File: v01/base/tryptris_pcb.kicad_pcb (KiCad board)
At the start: 2 copper layers, 298.8 x 122 mm, 141 parts, among them J1 USB_C_Receptacle_USB2.0, J2 I2C-L, J3 I2C-R, SW1 Reset, U1 ATmega32U4-AU, U2 MCP23017_SO, U4 HOLE, Y1 16Mhz

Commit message: Clean up base silk screen too.
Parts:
- moved G*** 1.35 mm to (251.4, 88.2)
- moved G*** 0.64 mm to (100.6, 88.5)

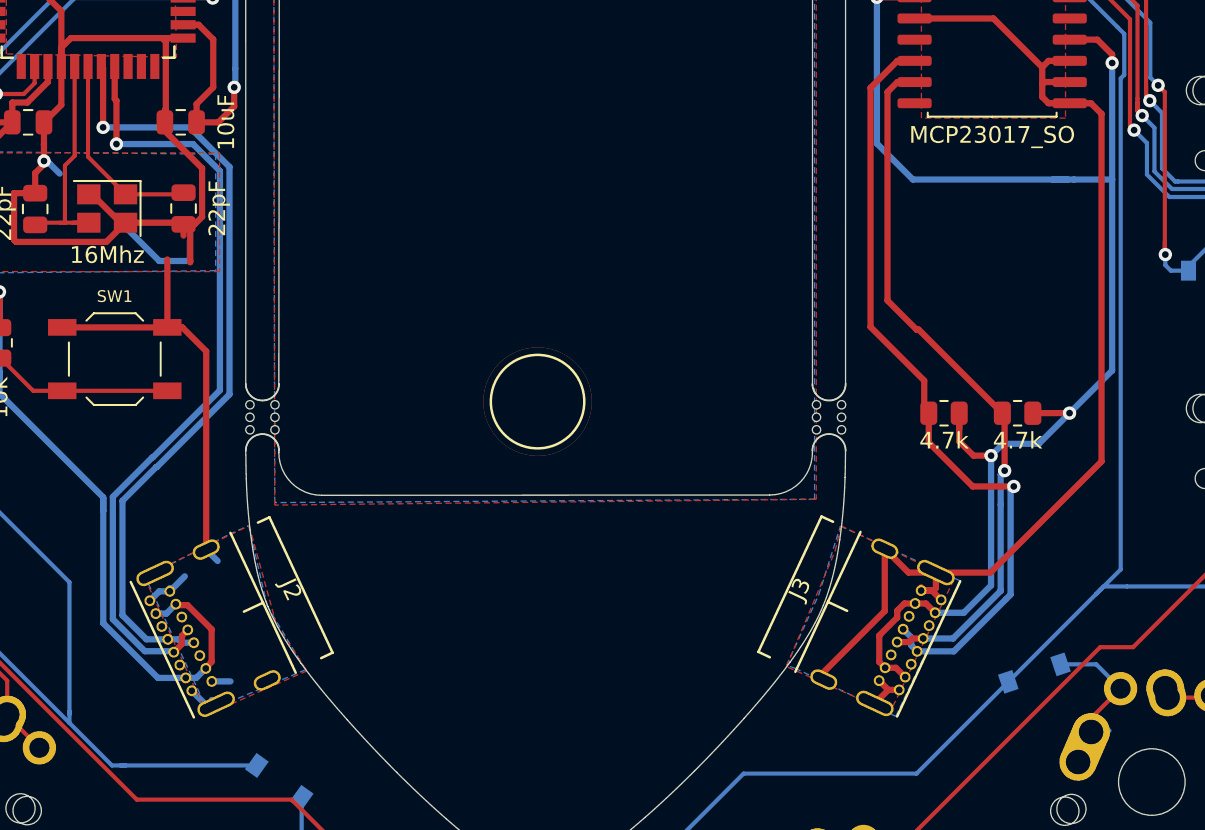
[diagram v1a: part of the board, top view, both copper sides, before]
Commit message: Move interconnect ports
I got some feedback that they might be tight for some cables. By sliding
the ports down a bit they can stay at the same angle and also give more
space for cable housing.
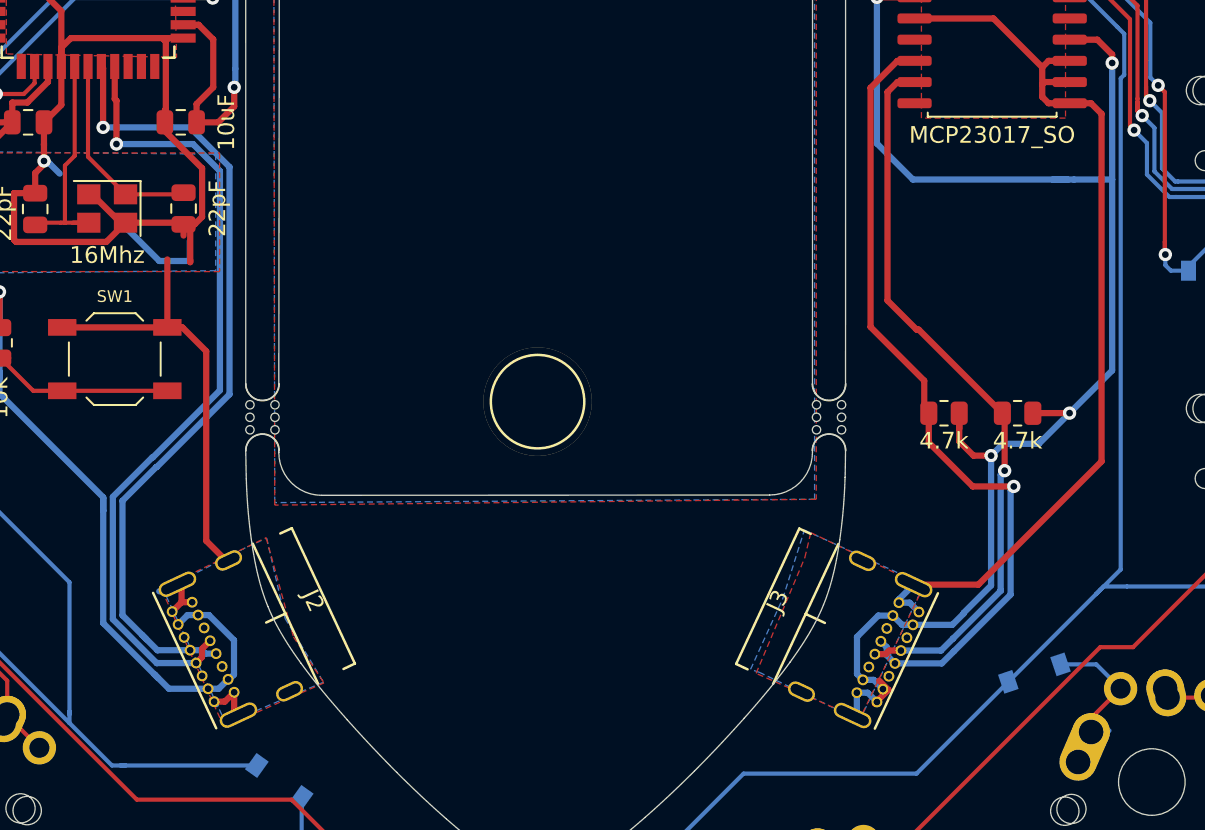
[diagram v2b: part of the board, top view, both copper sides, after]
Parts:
- moved J3 1.52 mm to (191.6, 114.4)
- moved J2 1.49 mm to (160.4, 114.4)
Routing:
- net VSS: track 70.8 -> 61.4 mm
- net SCL-L: track 46.9 -> 48.9 mm
- net GND: track 178.3 -> 180.2 mm
- net +5V: track 154.9 -> 156.7 mm
- net VBUS: track 85.1 -> 86.9 mm
- net SDA-R: track 42.3 -> 44.0 mm
- net SCL-R: track 47.4 -> 49.1 mm
- net SDA-L: track 47.3 -> 48.9 mm

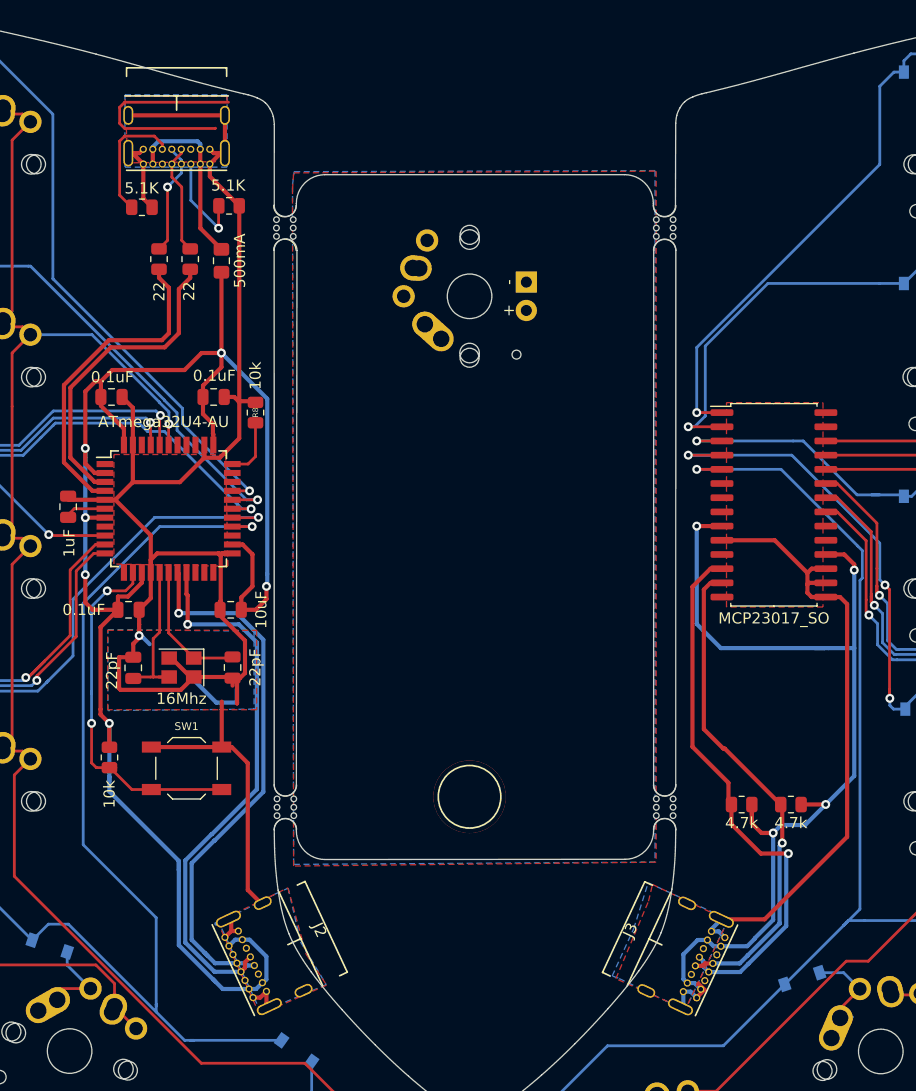
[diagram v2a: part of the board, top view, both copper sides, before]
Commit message: Update base model to use parts from lcsc
The footprints for USB ports had to change as I can't get the previous
footprint shape from lcsc.
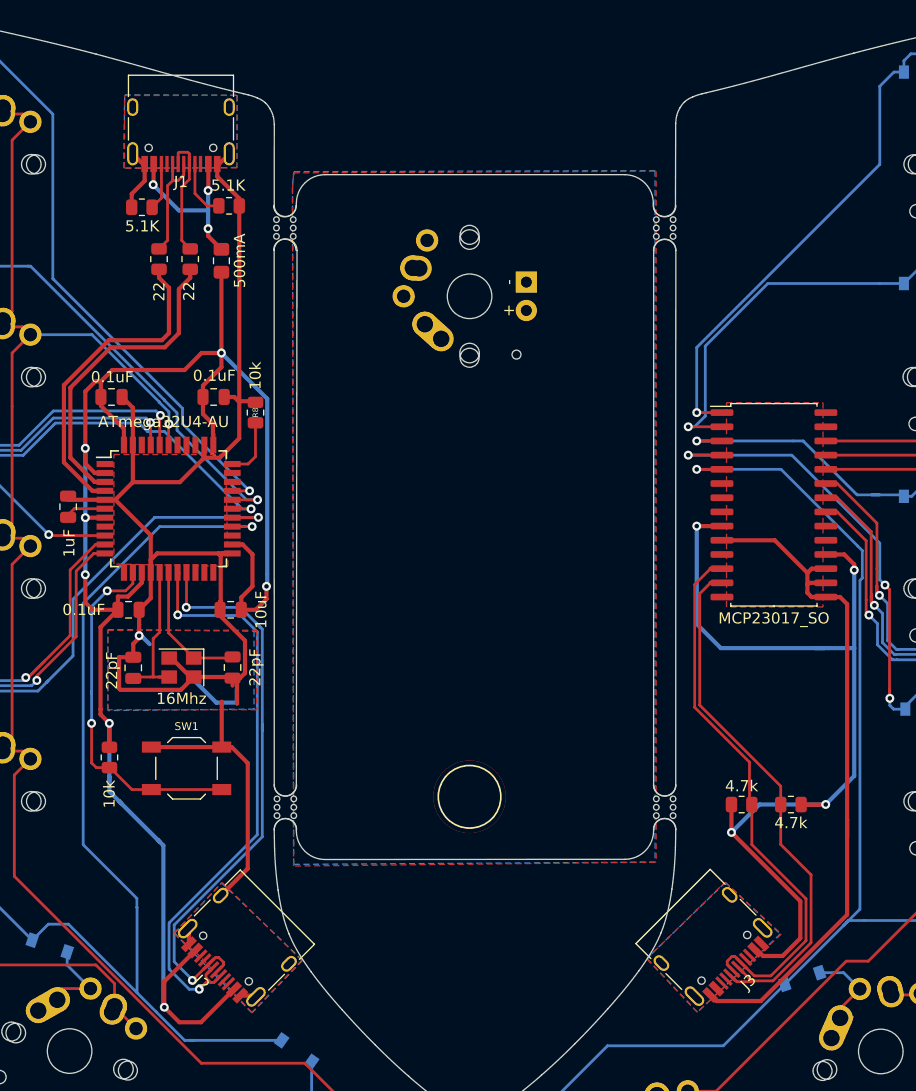
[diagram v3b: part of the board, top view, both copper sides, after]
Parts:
- J1, J2, J3: footprint Type-C:USB_C_GCT_USB4085 -> Connector_USB:USB_C_Receptacle_HRO_TYPE-C-31-M-12
- moved J3 4.91 mm to (196.5, 114.3), turned to 225 degrees
- moved J2 4.85 mm to (155.5, 114.3), turned to 135 degrees
- moved J1 2.09 mm to (149.7, 41.0)
- turned R3 to 180 degrees
- turned R6 to 180 degrees
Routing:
- net GND: track 180.2 -> 159.1 mm
- net (no net): track 20.2 -> 0.00 mm
- net Net-(J1-PadB5): track 11.1 -> 4.22 mm
- net SDA-R: track 44.0 -> 48.7 mm, vias 1 -> 0
- net SCL-L: track 48.9 -> 52.9 mm, vias 1 -> 2
- net SDA-L: track 48.9 -> 52.4 mm, vias 1 -> 2
- net Net-(J1-PadA5): track 8.77 -> 5.28 mm, vias 1 -> 0
- net VBUS: track 86.9 -> 83.9 mm
- net +5V: track 156.7 -> 159.4 mm, vias 6 -> 7
- net Row4-L: track 114.0 -> 111.4 mm
- net VSS: track 61.4 -> 63.0 mm
- net Net-(J1-PadA7): track 9.95 -> 11.2 mm
- net VCC: track 16.7 -> 16.3 mm, vias 0 -> 3
- net Net-(J1-PadA6): track 10.1 -> 10.3 mm, vias 1 -> 0
- net SCL-R: track 49.1 -> 49.0 mm, vias 1 -> 0

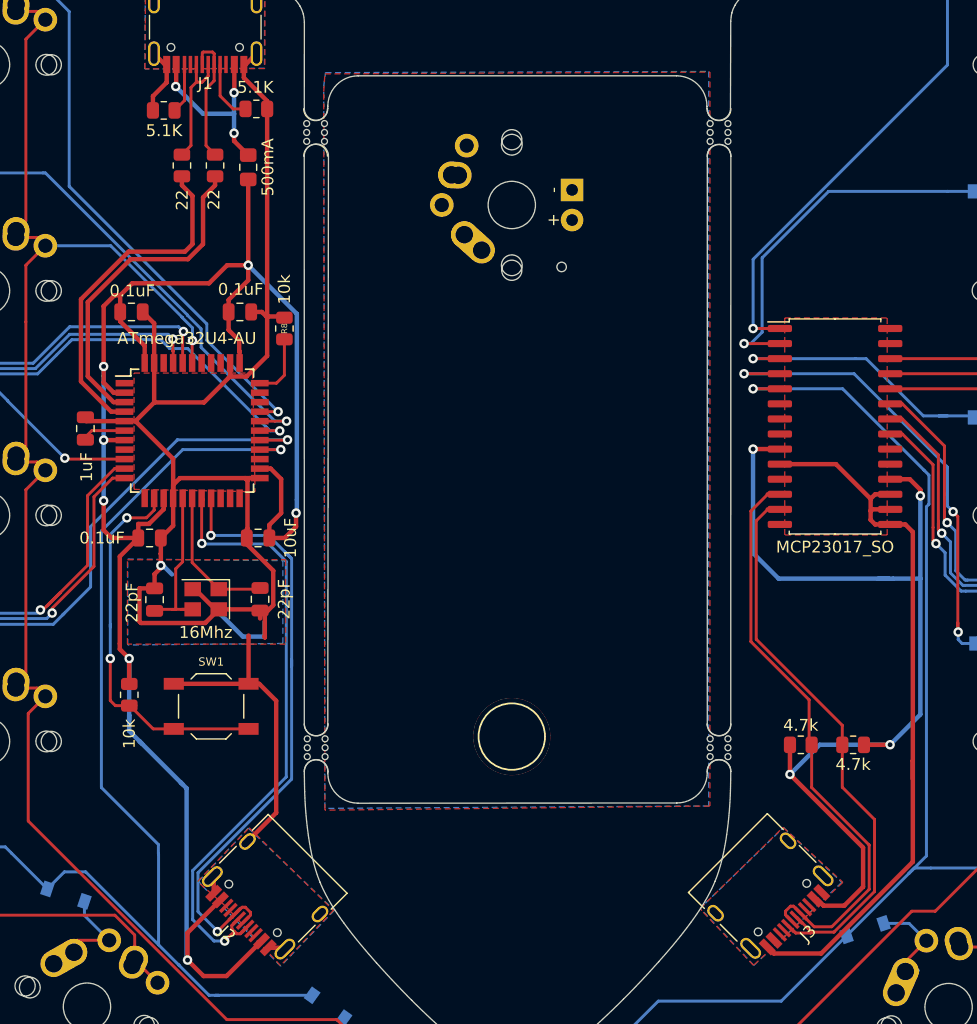
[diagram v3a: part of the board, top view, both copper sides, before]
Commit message: Tidy up silkscreen.
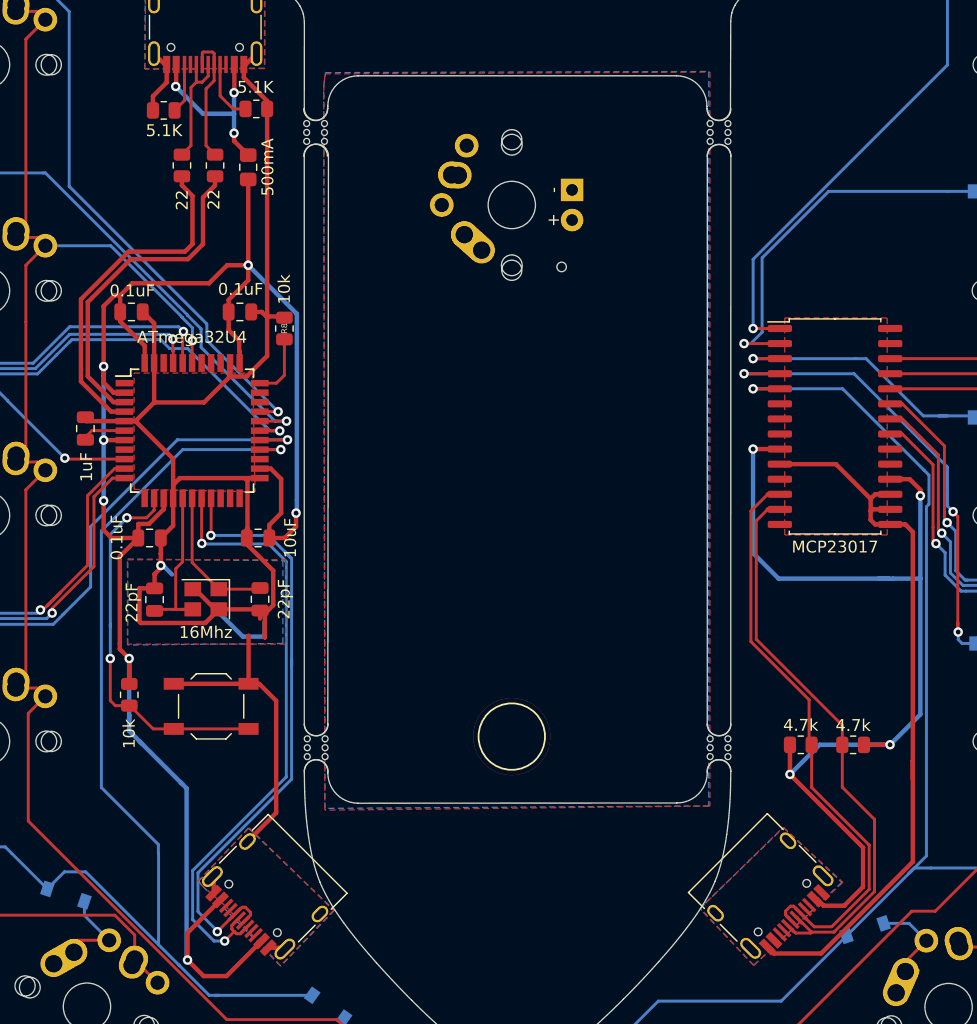
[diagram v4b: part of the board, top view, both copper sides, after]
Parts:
- U1: value ATmega32U4-AU -> ATmega32U4
- U2: value MCP23017_SO -> MCP23017
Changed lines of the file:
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@@
     (44 Edge.Cuts user)
     (45 Margin user)
-    (46 B.CrtYd user)
+    (46 B.CrtYd user hide)
     (47 F.CrtYd user hide)
     (48 B.Fab user hide)
@@
     (tags "usb usb-c 2.0 pd")
     (attr smd)
-    (fp_text reference J2 (at 0 -5.645 135) (layer F.SilkS)
+    (fp_text reference J2 (at 0 -5.645 135) (layer F.Fab)
       (effects (font (size 1 1) (thickness 0.15)))
     )
@@
     (tags "usb usb-c 2.0 pd")
     (attr smd)
-    (fp_text reference J3 (at 0 -5.645 45) (layer F.SilkS)
+    (fp_text reference J3 (at 0 -5.645 45) (layer F.Fab)
       (effects (font (size 1 1) (thickness 0.15)))
     )
@@
     (tags "usb usb-c 2.0 pd")
     (attr smd)
-    (fp_text reference J1 (at 0 -5.645) (layer F.SilkS)
+    (fp_text reference J1 (at 0 -5.645) (layer F.Fab)
       (effects (font (size 1 1) (thickness 0.15)))
     )
@@
       (effects (font (size 1 1) (thickness 0.15)))
     )
-    (fp_text value 4.7k (at 0 1.65) (layer F.SilkS)
+    (fp_text value 4.7k (at 0 -1.633201) (layer F.SilkS)
       (effects (font (size 1 1) (thickness 0.15)))
     )
@@
       (effects (font (size 1 1) (thickness 0.15)))
     )
-    (fp_text value MCP23017_SO (at 0 10.16 180) (layer F.SilkS)
+    (fp_text value MCP23017 (at 0 10.16 180) (layer F.SilkS)
       (effects (font (size 1 1) (thickness 0.15)))
     )
@@
       (effects (font (size 1 1) (thickness 0.15)))
     )
-    (fp_text value ATmega32U4-AU (at -0.45 -7.775) (layer F.SilkS)
+    (fp_text value ATmega32U4 (at -0.0101 -7.8694) (layer F.SilkS)
       (effects (font (size 1 1) (thickness 0.15)))
     )
@@
       (effects (font (size 1 1) (thickness 0.15)))
     )
-    (fp_text value 0.1uF (at -4.003 0 -180) (layer F.SilkS)
+    (fp_text value 0.1uF (at -2.7457 -0.0381 90) (layer F.SilkS)
       (effects (font (size 1 1) (thickness 0.15)))
     )
@@
     (tags "SPST Tactile Switch")
     (attr smd)
-    (fp_text reference SW1 (at 0 -3.75) (layer F.SilkS)
+    (fp_text reference SW1 (at 0 -3.75) (layer F.Fab)
       (effects (font (size 0.7 0.7) (thickness 0.15)))
     )

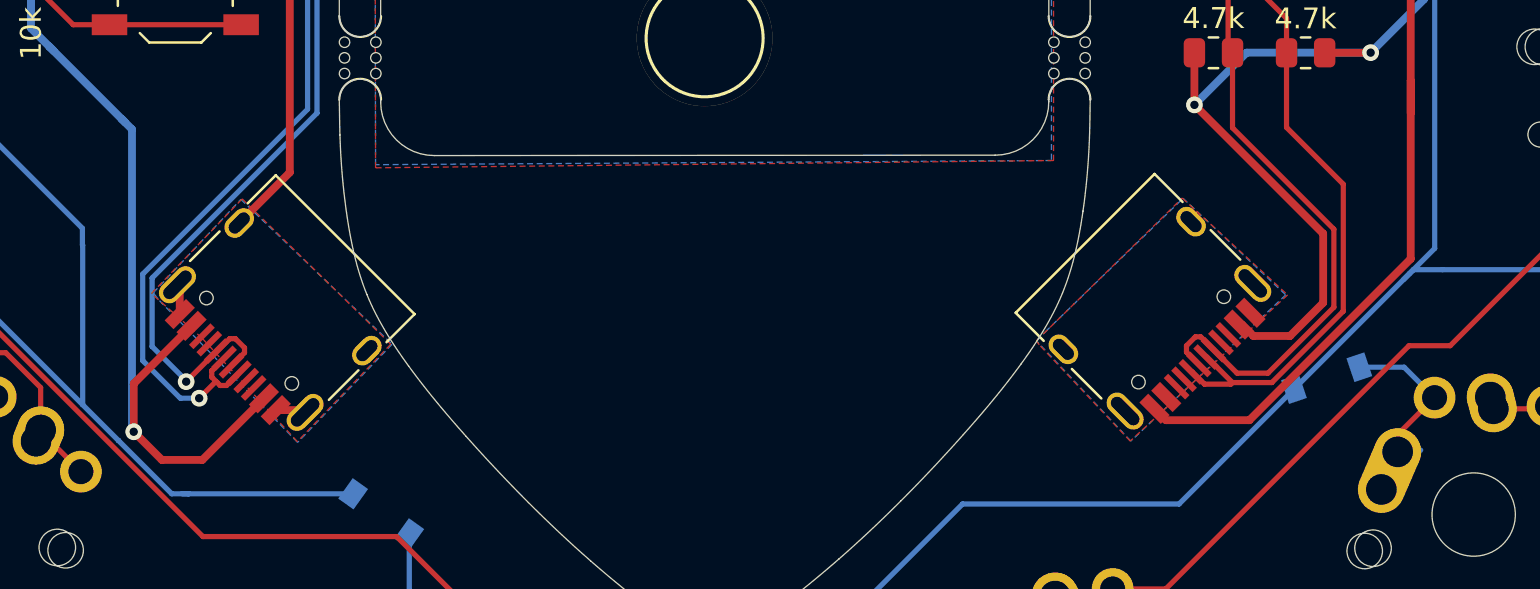
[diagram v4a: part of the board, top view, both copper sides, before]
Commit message: Use freeform routing to get USB ports in a better position.
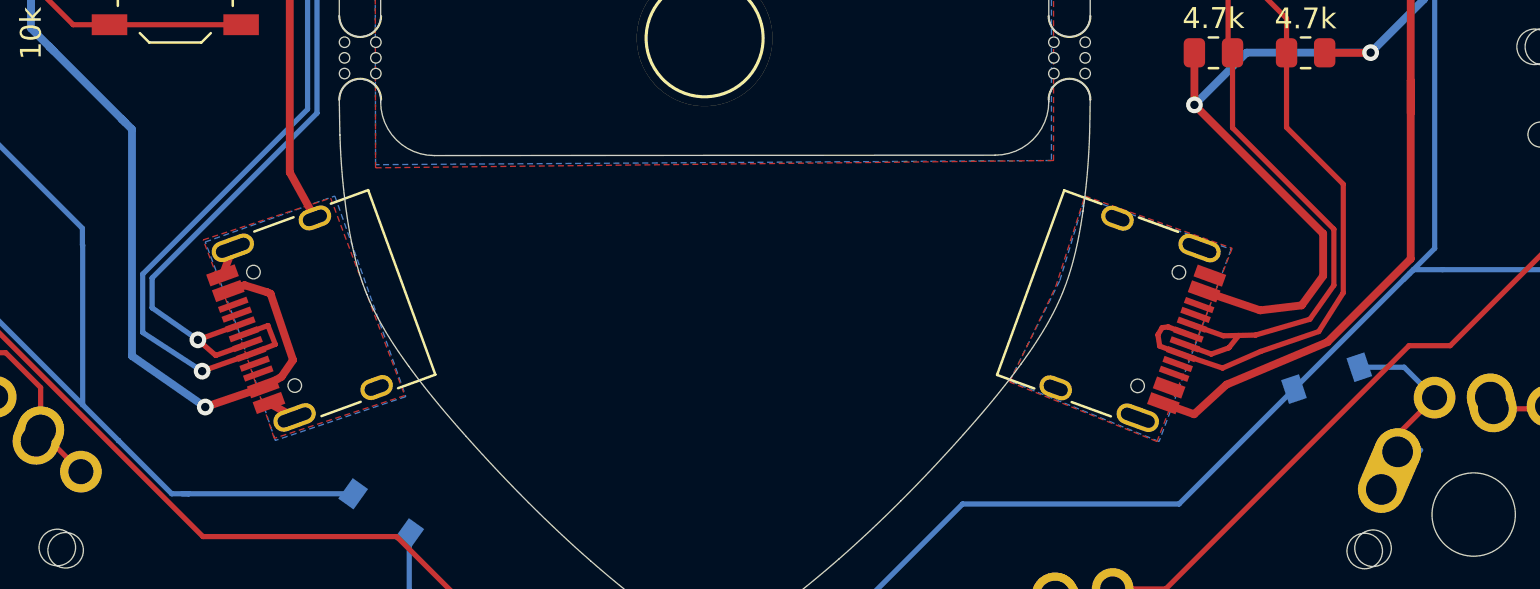
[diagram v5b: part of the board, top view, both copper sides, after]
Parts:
- moved J2 1.84 mm to (157.3, 114.7), turned to 110 degrees
- moved J3 1.76 mm to (194.8, 114.7), turned to 250 degrees
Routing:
- net +5V: track 159.4 -> 156.2 mm
- net SDA-L: track 52.4 -> 50.7 mm
- net VSS: track 63.0 -> 61.9 mm
- net GND: track 159.1 -> 158.1 mm
- net SDA-R: track 48.7 -> 49.7 mm
- net SCL-R: track 49.0 -> 48.4 mm
